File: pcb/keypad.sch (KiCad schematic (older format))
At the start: 8 parts, among them SW700 SW_Push, SW701 SW_Push, SW702 SW_Push, SW703 SW_Push, SW704 SW_Push, SW705 SW_Push, SW706 SW_Push, SW707 SW_Push

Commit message: finish sch rev 0.1
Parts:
- removed SW700, SW701, SW702: SW_Push, footprints:contact, symbol Switch:SW_Push
- SW700: renamed from SW703; footprint footprints:contact -> footprints:EVQQ2
- SW701: renamed from SW704; footprint footprints:contact -> footprints:EVQQ2
- SW702: renamed from SW705; footprint footprints:contact -> footprints:EVQQ2
- SW703: renamed from SW707; footprint footprints:contact -> footprints:EVQQ2
- SW704: renamed from SW706; footprint footprints:contact -> footprints:EVQQ2
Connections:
- net SW_B renamed SW_CE
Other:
- moved on the sheet: SW700, SW701, SW702, SW703, SW704
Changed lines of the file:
@@
 EESchema Schematic File Version 4
-LIBS:pcb-cache
 EELAYER 30 0
 EELAYER END
@@
 Comment4 ""
 $EndDescr
-Text GLabel 6000 3600 0    50   Output ~ 0
-SW_ST
-Text GLabel 5500 4500 0    50   Output ~ 0
+Text GLabel 5800 3500 0    50   Output ~ 0
 SW_RI
-Text GLabel 6900 4300 0    50   Output ~ 0
-SW_A
-Text GLabel 6500 4700 0    50   Output ~ 0
-SW_B
-Text GLabel 4500 4500 0    50   Output ~ 0
+Text GLabel 5000 3500 0    50   Output ~ 0
+SW_CE
+Text GLabel 4200 3500 0    50   Output ~ 0
 SW_LE
-Text GLabel 5000 4100 0    50   Output ~ 0
+Text GLabel 5000 3000 0    50   Output ~ 0
 SW_UP
-Text GLabel 5200 3600 0    50   Output ~ 0
-SW_SE
-Text GLabel 5000 4900 0    50   Output ~ 0
+Text GLabel 5000 4000 0    50   Output ~ 0
 SW_DN
 $Comp
 L power:GND #PWR0288
 U 1 1 5D28BC76
-P 5400 4100
-F 0 "#PWR0288" H 5400 3850 50  0001 C CNN
-F 1 "GND" H 5405 3927 50  0000 C CNN
-F 2 "" H 5400 4100 50  0001 C CNN
-F 3 "" H 5400 4100 50  0001 C CNN
-	1    5400 4100
+P 5400 3000
+F 0 "#PWR0288" H 5400 2750 50  0001 C CNN
+F 1 "GND" H 5405 2827 50  0000 C CNN
+F 2 "" H 5400 3000 50  0001 C CNN
+F 3 "" H 5400 3000 50  0001 C CNN
+	1    5400 3000
 	1    0    0    -1
 $EndComp
@@
 L power:GND #PWR0287
 U 1 1 5D28B91D
-P 4900 4500
-F 0 "#PWR0287" H 4900 4250 50  0001 C CNN
-F 1 "GND" H 4905 4327 50  0000 C CNN
-F 2 "" H 4900 4500 50  0001 C CNN
-F 3 "" H 4900 4500 50  0001 C CNN
-	1    4900 4500
+P 4600 3500
+F 0 "#PWR0287" H 4600 3250 50  0001 C CNN
+F 1 "GND" H 4605 3327 50  0000 C CNN
+F 2 "" H 4600 3500 50  0001 C CNN
+F 3 "" H 4600 3500 50  0001 C CNN
+	1    4600 3500
 	1    0    0    -1
 $EndComp
@@
 L power:GND #PWR0286
 U 1 1 5D28B509
-P 5400 4900
-F 0 "#PWR0286" H 5400 4650 50  0001 C CNN
-F 1 "GND" H 5405 4727 50  0000 C CNN
-F 2 "" H 5400 4900 50  0001 C CNN
-F 3 "" H 5400 4900 50  0001 C CNN
-	1    5400 4900
+P 5400 4000
+F 0 "#PWR0286" H 5400 3750 50  0001 C CNN
+F 1 "GND" H 5405 3827 50  0000 C CNN
+F 2 "" H 5400 4000 50  0001 C CNN
+F 3 "" H 5400 4000 50  0001 C CNN
+	1    5400 4000
 	1    0    0    -1
 $EndComp
@@
 L power:GND #PWR0285
 U 1 1 5D28B128
-P 5900 4500
-F 0 "#PWR0285" H 5900 4250 50  0001 C CNN
-F 1 "GND" H 5905 4327 50  0000 C CNN
-F 2 "" H 5900 4500 50  0001 C CNN
-F 3 "" H 5900 4500 50  0001 C CNN
-	1    5900 4500
+P 6200 3500
+F 0 "#PWR0285" H 6200 3250 50  0001 C CNN
+F 1 "GND" H 6205 3327 50  0000 C CNN
+F 2 "" H 6200 3500 50  0001 C CNN
+F 3 "" H 6200 3500 50  0001 C CNN
+	1    6200 3500
 	1    0    0    -1
 $EndComp
@@
 L power:GND #PWR0284
 U 1 1 5D28AD69
-P 6900 4700
-F 0 "#PWR0284" H 6900 4450 50  0001 C CNN
-F 1 "GND" H 6905 4527 50  0000 C CNN
-F 2 "" H 6900 4700 50  0001 C CNN
-F 3 "" H 6900 4700 50  0001 C CNN
-	1    6900 4700
+P 5400 3500
+F 0 "#PWR0284" H 5400 3250 50  0001 C CNN
+F 1 "GND" H 5405 3327 50  0000 C CNN
+F 2 "" H 5400 3500 50  0001 C CNN
+F 3 "" H 5400 3500 50  0001 C CNN
+	1    5400 3500
 	1    0    0    -1
 $EndComp
 $Comp
-L power:GND #PWR0283
-U 1 1 5D28AA10
-P 7300 4300
-F 0 "#PWR0283" H 7300 4050 50  0001 C CNN
-F 1 "GND" H 7305 4127 50  0000 C CNN
-F 2 "" H 7300 4300 50  0001 C CNN
-F 3 "" H 7300 4300 50  0001 C CNN
-	1    7300 4300
+L Switch:SW_Push SW700
+U 1 1 5D27EABD
+P 5200 3500
+F 0 "SW700" H 5200 3785 50  0000 C CNN
+F 1 "SW_Push" H 5200 3694 50  0000 C CNN
+F 2 "footprints:EVQQ2" H 5200 3700 50  0001 C CNN
+F 3 "~" H 5200 3700 50  0001 C CNN
+	1    5200 3500
 	1    0    0    -1
 $EndComp
 $Comp
-L power:GND #PWR0282
-U 1 1 5D289F76
-P 5600 3600
-F 0 "#PWR0282" H 5600 3350 50  0001 C CNN
-F 1 "GND" H 5605 3427 50  0000 C CNN
-F 2 "" H 5600 3600 50  0001 C CNN
-F 3 "" H 5600 3600 50  0001 C CNN
-	1    5600 3600
+L Switch:SW_Push SW704
+U 1 1 5D27D8DE
+P 6000 3500
+F 0 "SW704" H 6000 3785 50  0000 C CNN
+F 1 "SW_Push" H 6000 3694 50  0000 C CNN
+F 2 "footprints:EVQQ2" H 6000 3700 50  0001 C CNN
+F 3 "~" H 6000 3700 50  0001 C CNN
+	1    6000 3500
 	1    0    0    -1
 $EndComp
 $Comp
-L power:GND #PWR0281
-U 1 1 5D288EE2
-P 6400 3600
-F 0 "#PWR0281" H 6400 3350 50  0001 C CNN
-F 1 "GND" H 6405 3427 50  0000 C CNN
-F 2 "" H 6400 3600 50  0001 C CNN
-F 3 "" H 6400 3600 50  0001 C CNN
-	1    6400 3600
+L Switch:SW_Push SW703
+U 1 1 5D27CCB2
+P 5200 4000
+F 0 "SW703" H 5200 4285 50  0000 C CNN
+F 1 "SW_Push" H 5200 4194 50  0000 C CNN
+F 2 "footprints:EVQQ2" H 5200 4200 50  0001 C CNN
+F 3 "~" H 5200 4200 50  0001 C CNN
+	1    5200 4000
+	1    0    0    -1
+$EndComp
+$Comp
+L Switch:SW_Push SW702
+U 1 1 5D27BD89
+P 4400 3500
+F 0 "SW702" H 4400 3785 50  0000 C CNN
+F 1 "SW_Push" H 4400 3694 50  0000 C CNN
+F 2 "footprints:EVQQ2" H 4400 3700 50  0001 C CNN
+F 3 "~" H 4400 3700 50  0001 C CNN
+	1    4400 3500
 	1    0    0    -1
 $EndComp
 $Comp
 L Switch:SW_Push SW701
-U 1 1 5D2828BB
-P 6200 3600
-F 0 "SW701" H 6200 3885 50  0000 C CNN
-F 1 "SW_Push" H 6200 3794 50  0000 C CNN
-F 2 "footprints:contact" H 6200 3800 50  0001 C CNN
-F 3 "~" H 6200 3800 50  0001 C CNN
-	1    6200 3600
+U 1 1 5D2797BD
+P 5200 3000
+F 0 "SW701" H 5200 3285 50  0000 C CNN
+F 1 "SW_Push" H 5200 3194 50  0000 C CNN
+F 2 "footprints:EVQQ2" H 5200 3200 50  0001 C CNN
+F 3 "~" H 5200 3200 50  0001 C CNN
+	1    5200 3000
 	1    0    0    -1
 $EndComp
-$Comp
-L Switch:SW_Push SW700
-U 1 1 5D281FA3
-P 5400 3600
-F 0 "SW700" H 5400 3885 50  0000 C CNN
-F 1 "SW_Push" H 5400 3794 50  0000 C CNN
-F 2 "footprints:contact" H 5400 3800 50  0001 C CNN
-F 3 "~" H 5400 3800 50  0001 C CNN
-	1    5400 3600
-	1    0    0    -1
-$EndComp
-$Comp
-L Switch:SW_Push SW703
-U 1 1 5D27EABD
-P 6700 4700
-F 0 "SW703" H 6700 4985 50  0000 C CNN
-F 1 "SW_Push" H 6700 4894 50  0000 C CNN
-F 2 "footprints:contact" H 6700 4900 50  0001 C CNN
-F 3 "~" H 6700 4900 50  0001 C CNN
-	1    6700 4700
-	1    0    0    -1
-$EndComp
-$Comp
-L Switch:SW_Push SW702
-U 1 1 5D27E22C
-P 7100 4300
-F 0 "SW702" H 7100 4585 50  0000 C CNN
-F 1 "SW_Push" H 7100 4494 50  0000 C CNN
-F 2 "footprints:contact" H 7100 4500 50  0001 C CNN
-F 3 "~" H 7100 4500 50  0001 C CNN
-	1    7100 4300
-	1    0    0    -1
-$EndComp
-$Comp
-L Switch:SW_Push SW706
-U 1 1 5D27D8DE
-P 5700 4500
-F 0 "SW706" H 5700 4785 50  0000 C CNN
-F 1 "SW_Push" H 5700 4694 50  0000 C CNN
-F 2 "footprints:contact" H 5700 4700 50  0001 C CNN
-F 3 "~" H 5700 4700 50  0001 C CNN
-	1    5700 4500
-	1    0    0    -1
-$EndComp
-$Comp
-L Switch:SW_Push SW707
-U 1 1 5D27CCB2
-P 5200 4900
-F 0 "SW707" H 5200 5185 50  0000 C CNN
-F 1 "SW_Push" H 5200 5094 50  0000 C CNN
-F 2 "footprints:contact" H 5200 5100 50  0001 C CNN
-F 3 "~" H 5200 5100 50  0001 C CNN
-	1    5200 4900
-	1    0    0    -1
-$EndComp
-$Comp
-L Switch:SW_Push SW705
-U 1 1 5D27BD89
-P 4700 4500
-F 0 "SW705" H 4700 4785 50  0000 C CNN
-F 1 "SW_Push" H 4700 4694 50  0000 C CNN
-F 2 "footprints:contact" H 4700 4700 50  0001 C CNN
-F 3 "~" H 4700 4700 50  0001 C CNN
-	1    4700 4500
-	1    0    0    -1
-$EndComp
-$Comp
-L Switch:SW_Push SW704
-U 1 1 5D2797BD
-P 5200 4100
-F 0 "SW704" H 5200 4385 50  0000 C CNN
-F 1 "SW_Push" H 5200 4294 50  0000 C CNN
-F 2 "footprints:contact" H 5200 4300 50  0001 C CNN
-F 3 "~" H 5200 4300 50  0001 C CNN
-	1    5200 4100
-	1    0    0    -1
-$EndComp

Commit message: rev 0.1
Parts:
- removed SW700: SW_Push, footprints:EVQQ2, symbol Switch:SW_Push
- SW701, SW702, SW703, SW704: footprint footprints:EVQQ2 -> Button_Switch_SMD:SW_SPST_EVQP7C
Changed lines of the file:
@@
 Text GLabel 5800 3500 0    50   Output ~ 0
 SW_RI
-Text GLabel 5000 3500 0    50   Output ~ 0
-SW_CE
 Text GLabel 4200 3500 0    50   Output ~ 0
 SW_LE
@@
 $EndComp
 $Comp
-L power:GND #PWR0284
-U 1 1 5D28AD69
-P 5400 3500
-F 0 "#PWR0284" H 5400 3250 50  0001 C CNN
-F 1 "GND" H 5405 3327 50  0000 C CNN
-F 2 "" H 5400 3500 50  0001 C CNN
-F 3 "" H 5400 3500 50  0001 C CNN
-	1    5400 3500
-	1    0    0    -1
-$EndComp
-$Comp
-L Switch:SW_Push SW700
-U 1 1 5D27EABD
-P 5200 3500
-F 0 "SW700" H 5200 3785 50  0000 C CNN
-F 1 "SW_Push" H 5200 3694 50  0000 C CNN
-F 2 "footprints:EVQQ2" H 5200 3700 50  0001 C CNN
-F 3 "~" H 5200 3700 50  0001 C CNN
-	1    5200 3500
-	1    0    0    -1
-$EndComp
-$Comp
 L Switch:SW_Push SW704
 U 1 1 5D27D8DE
@@
 F 0 "SW704" H 6000 3785 50  0000 C CNN
 F 1 "SW_Push" H 6000 3694 50  0000 C CNN
-F 2 "footprints:EVQQ2" H 6000 3700 50  0001 C CNN
+F 2 "Button_Switch_SMD:SW_SPST_EVQP7C" H 6000 3700 50  0001 C CNN
 F 3 "~" H 6000 3700 50  0001 C CNN
 	1    6000 3500
@@
 F 0 "SW703" H 5200 4285 50  0000 C CNN
 F 1 "SW_Push" H 5200 4194 50  0000 C CNN
-F 2 "footprints:EVQQ2" H 5200 4200 50  0001 C CNN
+F 2 "Button_Switch_SMD:SW_SPST_EVQP7C" H 5200 4200 50  0001 C CNN
 F 3 "~" H 5200 4200 50  0001 C CNN
 	1    5200 4000
@@
 F 0 "SW702" H 4400 3785 50  0000 C CNN
 F 1 "SW_Push" H 4400 3694 50  0000 C CNN
-F 2 "footprints:EVQQ2" H 4400 3700 50  0001 C CNN
+F 2 "Button_Switch_SMD:SW_SPST_EVQP7C" H 4400 3700 50  0001 C CNN
 F 3 "~" H 4400 3700 50  0001 C CNN
 	1    4400 3500
@@
 F 0 "SW701" H 5200 3285 50  0000 C CNN
 F 1 "SW_Push" H 5200 3194 50  0000 C CNN
-F 2 "footprints:EVQQ2" H 5200 3200 50  0001 C CNN
+F 2 "Button_Switch_SMD:SW_SPST_EVQP7C" H 5200 3200 50  0001 C CNN
 F 3 "~" H 5200 3200 50  0001 C CNN
 	1    5200 3000

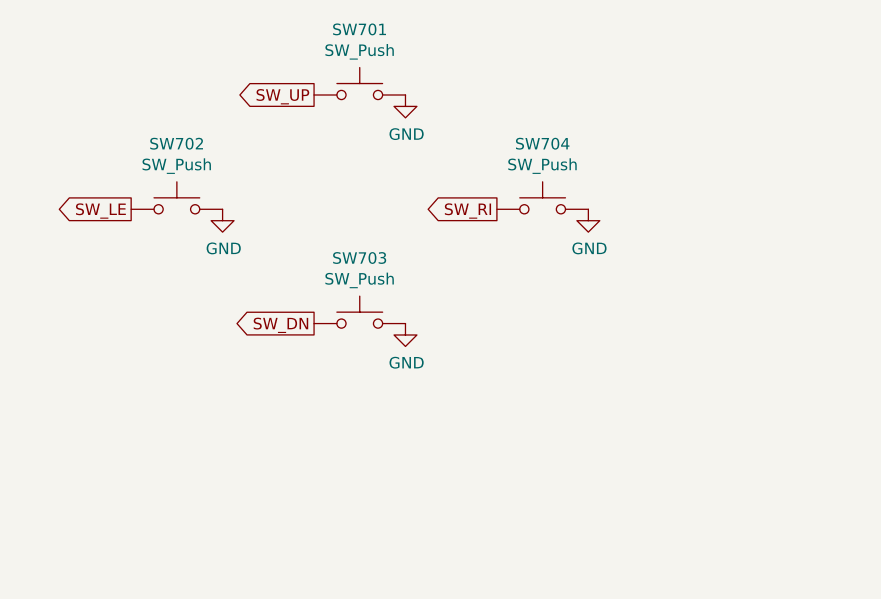
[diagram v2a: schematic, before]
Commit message: pcb: rename keypad signal names
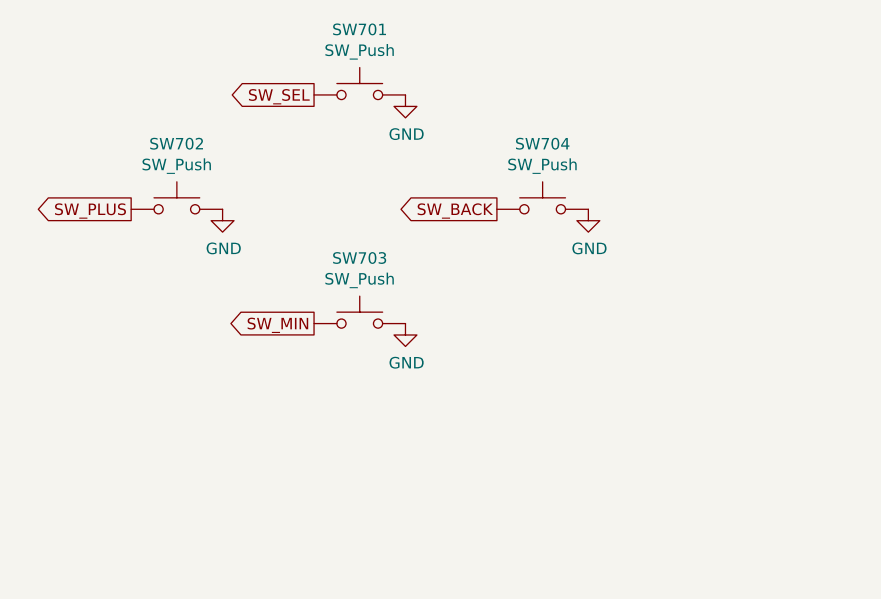
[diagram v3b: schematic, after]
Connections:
- net SW_DN renamed SW_MIN
- net SW_LE renamed SW_PLUS
- net SW_RI renamed SW_BACK
- net SW_UP renamed SW_SEL
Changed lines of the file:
@@
 $EndDescr
 Text GLabel 5800 3500 0    50   Output ~ 0
-SW_RI
+SW_BACK
 Text GLabel 4200 3500 0    50   Output ~ 0
-SW_LE
+SW_PLUS
 Text GLabel 5000 3000 0    50   Output ~ 0
-SW_UP
+SW_SEL
 Text GLabel 5000 4000 0    50   Output ~ 0
-SW_DN
+SW_MIN
 $Comp
 L power:GND #PWR0288
